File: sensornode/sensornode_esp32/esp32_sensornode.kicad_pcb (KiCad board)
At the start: 2 copper layers, 70 x 33 mm, 38 parts, among them J1 Conn_01x06_Female, J2 Conn_01x07_Male, J3 Micro_SD_Card, J4 USB_B_Mini, J5 Conn_01x02_Male, J6 Conn_02x03_Odd_Even, J7 Conn_02x03_Odd_Even, Q1 NDS3332P, Q2 NDS3332P, Q3 NDS3332P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

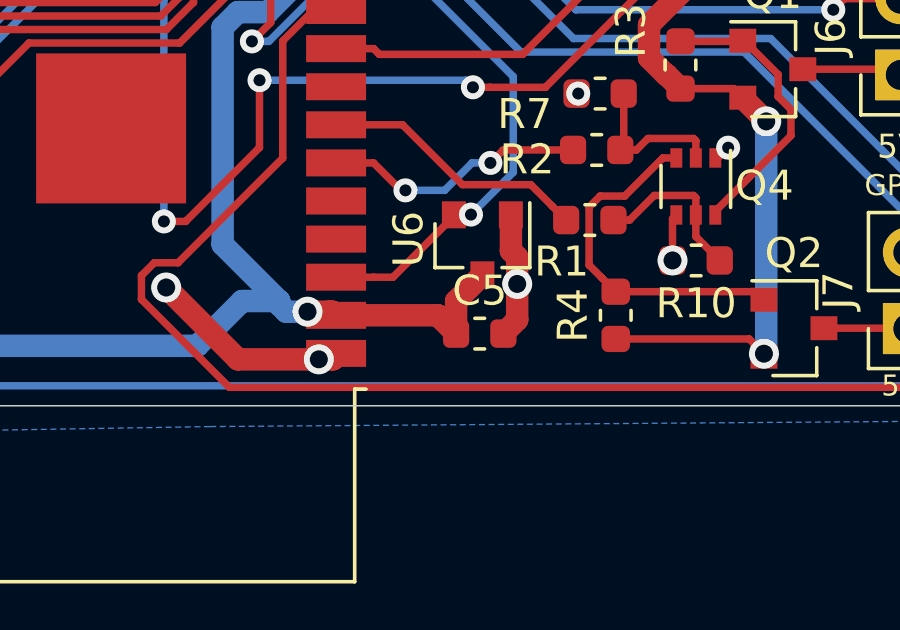
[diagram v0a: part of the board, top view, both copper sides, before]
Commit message: update parts to use all 0603, move labels to be legible
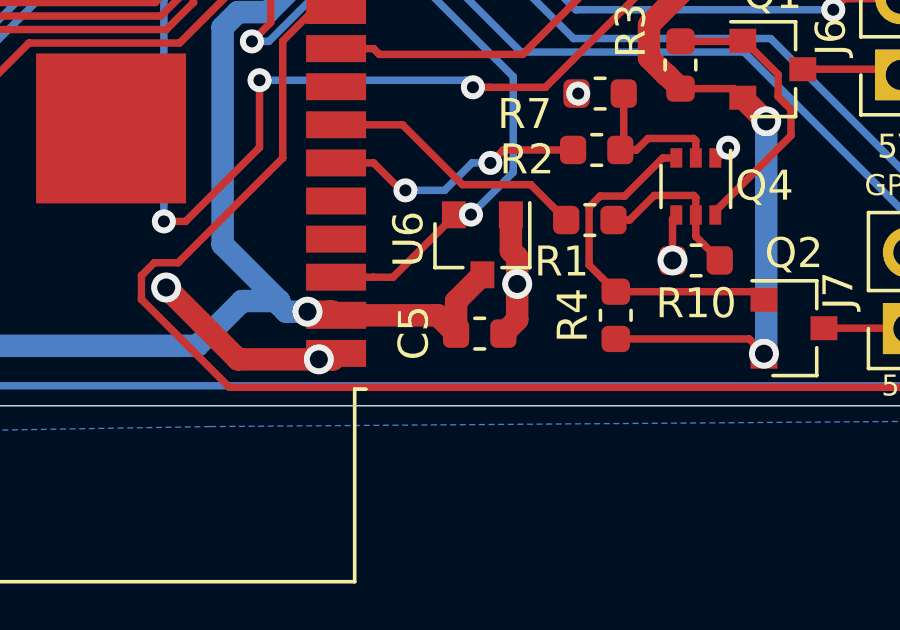
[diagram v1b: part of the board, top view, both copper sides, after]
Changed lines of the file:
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@@
       (outputformat 1)
       (mirror false)
-      (drillshape 1)
+      (drillshape 0)
       (scaleselection 1)
       (outputdirectory ""))
@@
     (tags capacitor)
     (attr smd)
-    (fp_text reference C5 (at 0 -1.43) (layer F.SilkS)
-      (effects (font (size 1 1) (thickness 0.15)))
-    )
+    (fp_text reference C5 (at -2.1971 -0.0254 90) (layer F.SilkS)
+      (effects (font (size 1 1) (thickness 0.15)))
+    )
